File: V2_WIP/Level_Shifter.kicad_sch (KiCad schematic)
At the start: 7 parts, among them U9 TCA39306DDFR

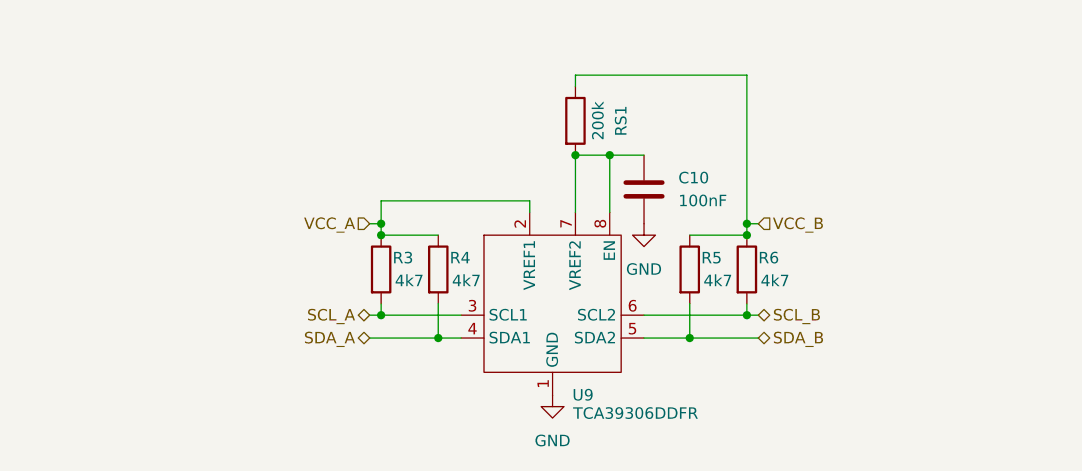
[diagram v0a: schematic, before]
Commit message: switched esp modul symbol for esp sheet
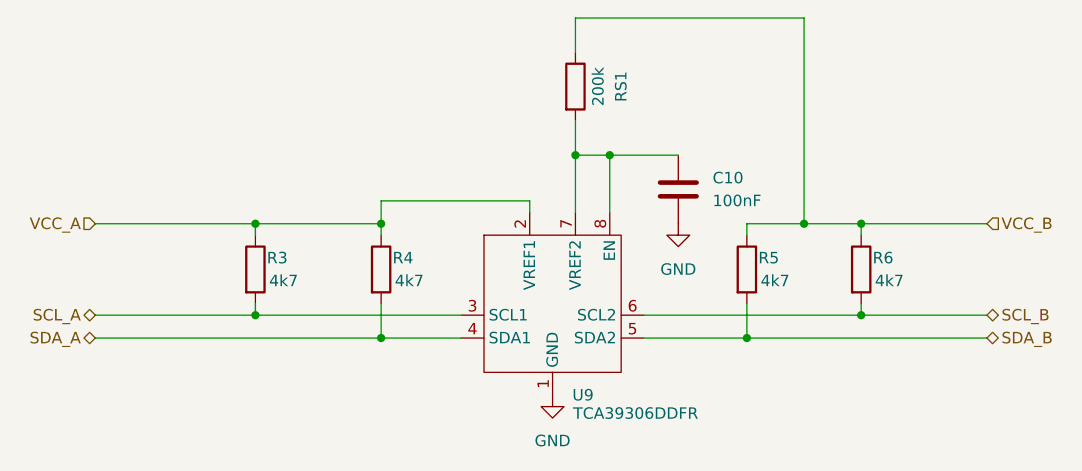
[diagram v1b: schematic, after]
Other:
- moved on the sheet: C10, R3, R4, R5, R6, RS1

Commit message: fixed errors in schematic
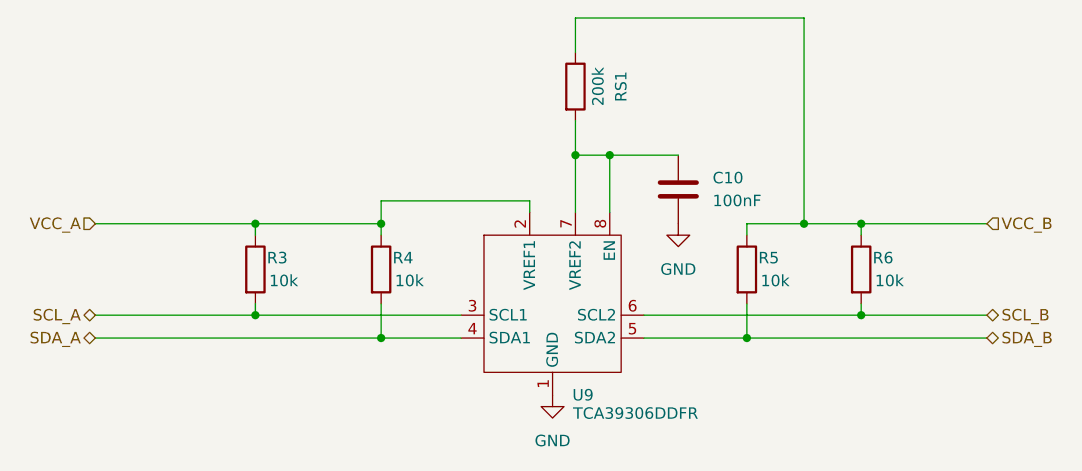
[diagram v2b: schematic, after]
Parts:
- R3, R4, R5, R6: value 4k7 -> 10k; footprint Resistor_SMD:R_0805_2012Metric_Pad1.20x1.40mm_HandSolder -> Resistor_SMD:R_0603_1608Metric_Pad0.98x0.95mm_HandSolder
- RS1: footprint Resistor_SMD:R_0805_2012Metric_Pad1.20x1.40mm_HandSolder -> Resistor_SMD:R_0603_1608Metric_Pad0.98x0.95mm_HandSolder
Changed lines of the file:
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@@
 			)
 		)
-		(property "Value" "4k7"
+		(property "Value" "10k"
 			(at 170.434 100.33 0)
 			(effects
@@
 			)
 		)
-		(property "Footprint" "Resistor_SMD:R_0805_2012Metric_Pad1.20x1.40mm_HandSolder"
+		(property "Footprint" "Resistor_SMD:R_0603_1608Metric_Pad0.98x0.95mm_HandSolder"
 			(at 167.132 99.06 90)
 			(effects
@@
 			)
 		)
-		(property "Footprint" "Resistor_SMD:R_0805_2012Metric_Pad1.20x1.40mm_HandSolder"
+		(property "Footprint" "Resistor_SMD:R_0603_1608Metric_Pad0.98x0.95mm_HandSolder"
 			(at 148.082 78.74 90)
 			(effects
@@
 			)
 		)
-		(property "Value" "4k7"
+		(property "Value" "10k"
 			(at 129.794 100.33 0)
 			(effects
@@
 			)
 		)
-		(property "Footprint" "Resistor_SMD:R_0805_2012Metric_Pad1.20x1.40mm_HandSolder"
+		(property "Footprint" "Resistor_SMD:R_0603_1608Metric_Pad0.98x0.95mm_HandSolder"
 			(at 126.492 99.06 90)
 			(effects
@@
 			)
 		)
-		(property "Value" "4k7"
+		(property "Value" "10k"
 			(at 115.824 100.33 0)
 			(effects
@@
 			)
 		)
-		(property "Footprint" "Resistor_SMD:R_0805_2012Metric_Pad1.20x1.40mm_HandSolder"
+		(property "Footprint" "Resistor_SMD:R_0603_1608Metric_Pad0.98x0.95mm_HandSolder"
 			(at 112.522 99.06 90)
 			(effects
@@
 			)
 		)
-		(property "Value" "4k7"
+		(property "Value" "10k"
 			(at 183.134 100.33 0)
 			(effects
@@
 			)
 		)
-		(property "Footprint" "Resistor_SMD:R_0805_2012Metric_Pad1.20x1.40mm_HandSolder"
+		(property "Footprint" "Resistor_SMD:R_0603_1608Metric_Pad0.98x0.95mm_HandSolder"
 			(at 179.832 99.06 90)
 			(effects

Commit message: updated most datashets
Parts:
- C10: footprint Capacitor_SMD:C_0805_2012Metric_Pad1.18x1.45mm_HandSolder -> Capacitor_SMD:C_0603_1608Metric_Pad1.08x0.95mm_HandSolder
- U9: value TCA39306DDFR -> *TCA39306DDFR
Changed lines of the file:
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@@
 			)
 		)
-		(property "Datasheet" "~"
+		(property "Datasheet" "https://cz.mouser.com/ProductDetail/SEI-Stackpole/RNCE0603BTE10K0?qs=sGAEpiMZZMtlubZbdhIBIGfmJML7fLMVDBbNntjsT8g%3D"
 			(at 168.91 99.06 0)
 			(effects
@@
 			)
 		)
+		(property "Purchase-URL" ""
+			(at 168.91 99.06 0)
+			(effects
+				(font
+					(size 1.27 1.27)
+				)
+				(hide yes)
+			)
+		)
 		(pin "1"
 		)
@@
 			)
 		)
-		(property "Datasheet" "~"
+		(property "Datasheet" "https://cz.mouser.com/ProductDetail/Vishay/TNPW0603200KBEEA?qs=sGAEpiMZZMtlubZbdhIBIGj%252BoYMmnMAlcFBCoPAeJRM%3D"
 			(at 149.86 78.74 0)
 			(effects
@@
 			)
 		)
+		(property "Purchase-URL" ""
+			(at 149.86 78.74 0)
+			(effects
+				(font
+					(size 1.27 1.27)
+				)
+				(hide yes)
+			)
+		)
 		(pin "1"
 		)
@@
 			)
 		)
-		(property "Datasheet" "~"
+		(property "Datasheet" "https://cz.mouser.com/ProductDetail/SEI-Stackpole/RNCE0603BTE10K0?qs=sGAEpiMZZMtlubZbdhIBIGfmJML7fLMVDBbNntjsT8g%3D"
 			(at 128.27 99.06 0)
 			(effects
@@
 			)
 		)
+		(property "Purchase-URL" ""
+			(at 128.27 99.06 0)
+			(effects
+				(font
+					(size 1.27 1.27)
+				)
+				(hide yes)
+			)
+		)
 		(pin "1"
 		)
@@
 			)
 		)
-		(property "Datasheet" "~"
+		(property "Datasheet" "https://cz.mouser.com/ProductDetail/SEI-Stackpole/RNCE0603BTE10K0?qs=sGAEpiMZZMtlubZbdhIBIGfmJML7fLMVDBbNntjsT8g%3D"
 			(at 114.3 99.06 0)
 			(effects
@@
 			)
 		)
+		(property "Purchase-URL" ""
+			(at 114.3 99.06 0)
+			(effects
+				(font
+					(size 1.27 1.27)
+				)
+				(hide yes)
+			)
+		)
 		(pin "1"
 		)
@@
 			)
 		)
-		(property "Value" "TCA39306DDFR"
+		(property "Value" "*TCA39306DDFR"
 			(at 149.606 115.062 0)
 			(effects
@@
 			)
 		)
+		(property "Purchase-URL" ""
+			(at 147.32 102.87 0)
+			(effects
+				(font
+					(size 1.27 1.27)
+				)
+				(hide yes)
+			)
+		)
 		(pin "1"
 		)
@@
 			)
 		)
-		(property "Datasheet" "~"
+		(property "Datasheet" "https://cz.mouser.com/ProductDetail/SEI-Stackpole/RNCE0603BTE10K0?qs=sGAEpiMZZMtlubZbdhIBIGfmJML7fLMVDBbNntjsT8g%3D"
 			(at 181.61 99.06 0)
 			(effects
@@
 		)
 		(property "Description" "Resistor"
+			(at 181.61 99.06 0)
+			(effects
+				(font
+					(size 1.27 1.27)
+				)
+				(hide yes)
+			)
+		)
+		(property "Purchase-URL" ""
 			(at 181.61 99.06 0)
 			(effects
@@
 			)
 		)
-		(property "Footprint" "Capacitor_SMD:C_0805_2012Metric_Pad1.18x1.45mm_HandSolder"
+		(property "Footprint" "Capacitor_SMD:C_0603_1608Metric_Pad1.08x0.95mm_HandSolder"
 			(at 160.3248 86.36 0)
 			(effects
@@
 			)
 		)
-		(property "Datasheet" "~"
+		(property "Datasheet" "https://cz.mouser.com/ProductDetail/KYOCERA-AVX/0603ZG104ZAT2A?qs=XWDBCzcA0Tke70DI9cEVbA%3D%3D"
 			(at 161.29 90.17 0)
 			(effects
@@
 			(at 161.29 90.17 0)
 			(effects
+				(font
+					(size 1.27 1.27)
+				)
+				(hide yes)
+			)
+		)
+		(property "Purchase-URL" ""
+			(at 161.29 90.17 0)
+			(effects
